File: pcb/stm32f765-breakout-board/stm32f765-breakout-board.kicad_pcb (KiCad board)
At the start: 2 copper layers, 50 x 50 mm, 39 parts, among them J1 16P_USB_C, J3 SWD, J4 Conn_01x05, J5 Conn_01x04, J6 Conn_01x12, J7 Conn_01x12, J8 Conn_01x03, J9 Conn_I2C2, SW2 SW_BOOT0, U1 STM32F765VIT6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

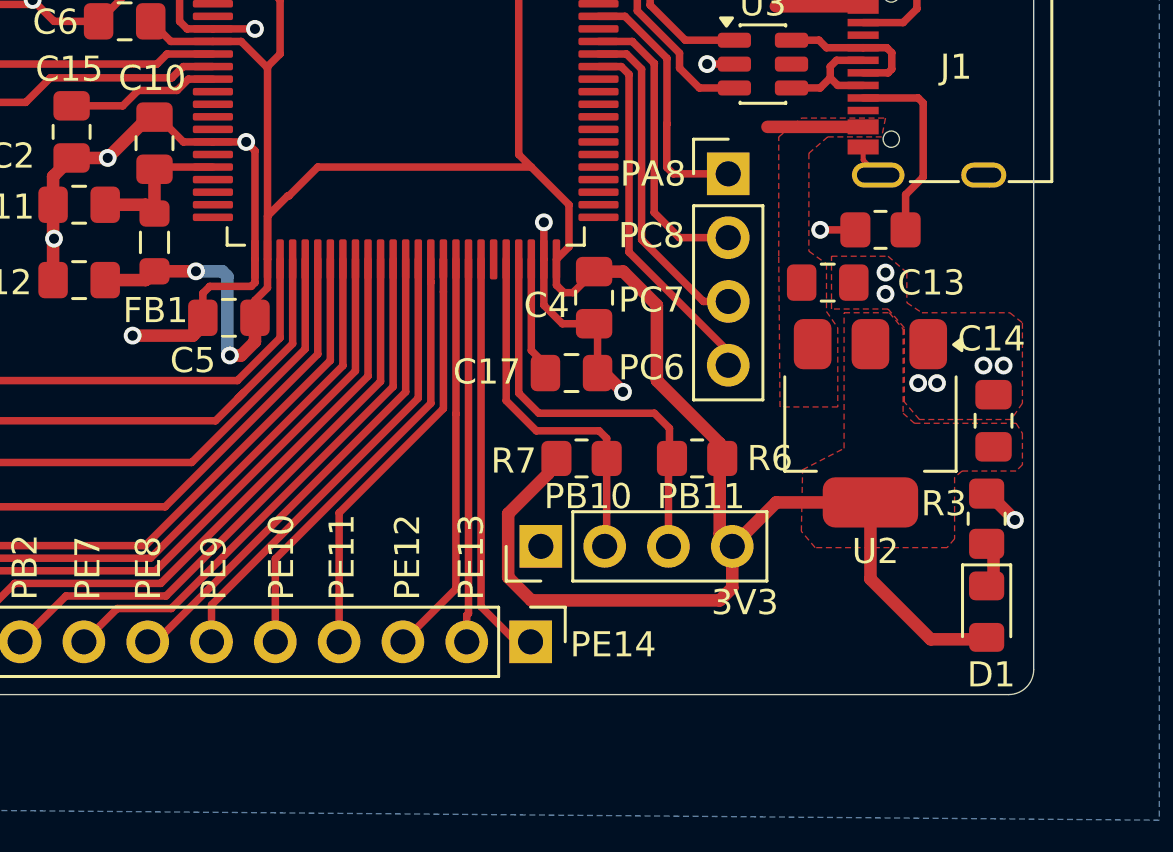
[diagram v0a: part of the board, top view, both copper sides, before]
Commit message: added lsm6dsl to pcb and ordered v3
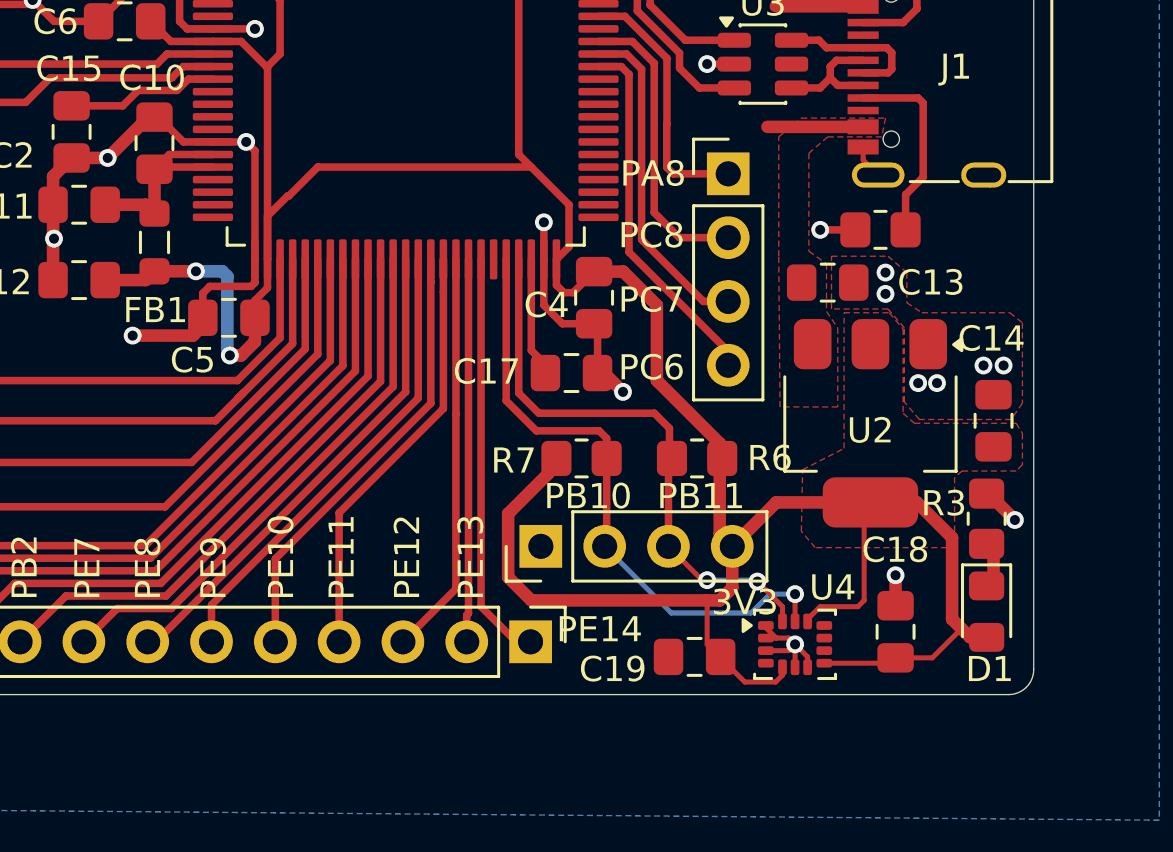
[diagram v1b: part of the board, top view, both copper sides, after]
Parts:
- added C18: 100n, Capacitor_SMD:C_0805_2012Metric_Pad1.18x1.45mm_HandSolder, F.Cu at (144.5, 147.5)
- added C19: 100n, Capacitor_SMD:C_0805_2012Metric_Pad1.18x1.45mm_HandSolder, F.Cu at (136.5, 148.5)
- added U4: LSM6DSL, Package_LGA:LGA-14_3x2.5mm_P0.5mm_LayoutBorder3x4y, F.Cu at (140.5, 148.0)
- R6, R7: value 1k5 -> 10k
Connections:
- U1 pad 20: unconnected-(U1-VREF+-Pad20) -> +3.3VA
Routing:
- net +3V3: track 180.2 -> 198.8 mm
- net I2C2_SCL: track 14.9 -> 25.0 mm, vias 0 -> 1
- net GND: track 90.2 -> 96.7 mm, vias 23 -> 25
- net I2C2_SDA: track 16.7 -> 22.8 mm, vias 0 -> 2
- net +3.3VA: track 6.23 -> 8.80 mm

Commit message: final breakout board ordered
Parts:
- added H1: MountingHole_Pad, MountingHole:MountingHole_2.2mm_M2_Pad, F.Cu at (103.5, 105.5)
- G***: moved to B.Cu
- moved G*** 28.3 mm to (124.8, 124.2), turned to 180 degrees
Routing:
- net VBUS: track 7.91 -> 14.1 mm

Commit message: Updated titleblock on f765 breakout pcb
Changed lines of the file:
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@@
 	)
 	(paper "A4")
+	(title_block
+		(title "STM32F765VIT6 Breakout Board")
+		(date "2026-04-17")
+		(rev "v5")
+		(company "Pranav Chandra N. V.")
+		(comment 1 "v2: Updated placement to gpio headers")
+		(comment 2 "v3: Properly grounded VCAP pins")
+		(comment 3 "v4: Rounded corners and changed silkscreen")
+		(comment 4 "v5: Updated titleblock")
+	)
 	(layers
 		(0 "F.Cu" signal)
@@
 		(embedded_fonts no)
 	)
+	(gr_circle
+		(center 119.25 119.25)
+		(end 119.5 119.5)
+		(stroke
+			(width 0.1)
+			(type solid)
+		)
+		(fill yes)
+		(layer "F.SilkS")
+	)
 	(gr_line

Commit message: Added on board LED to PCB and blinky for board
v6 of the PCB now has an in built on board LED to PE02, to allow for
faster debugging.

The first assembled prototype finally worked, and a blinky sketch was
flashed to test. Relevant code has been added to firmware.
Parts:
- added D2: LED, LED_SMD:LED_0805_2012Metric_Pad1.15x1.40mm_HandSolder, F.Cu at (125.0, 79.6)
- added R1: 1k5, Resistor_SMD:R_0805_2012Metric_Pad1.20x1.40mm_HandSolder, F.Cu at (129.7, 81.7)
- C13, C14: value 100n -> 22u
- H1: value MountingHole_Pad -> GND
- moved C16 37.5 mm to (153.4, 84.6)
- moved C2 37.5 mm to (123.7, 93.7)
- moved J4 37.5 mm to (118.2, 107.3)
- moved Y1 37.5 mm to (120.2, 91.2)
- moved C10 37.5 mm to (131.2, 94.2)
- moved C3 37.5 mm to (150.4, 83.7)
- moved C7 37.5 mm to (130.0, 87.1)
- moved D1 37.5 mm to (164.3, 112.9)
- moved J5 37.5 mm to (154.0, 95.5)
- moved J6 37.5 mm to (146.2, 114.1)
- moved J7 37.5 mm to (136.3, 68.2)
- moved J9 37.5 mm to (146.6, 110.3)
- moved R5 37.5 mm to (160.2, 84.8)
- moved R6 37.5 mm to (152.8, 106.8)
- moved C1 37.5 mm to (123.7, 89.8)
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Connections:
- U1 pad 1: unconnected-(U1-PE2-Pad1) -> PE02
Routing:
- net PE02: track 0.00 -> 4.78 mm
- net /Peripherals/OB_LED: track 0.00 -> 3.66 mm
- net GND: track 96.7 -> 98.7 mm, vias 25 -> 26
